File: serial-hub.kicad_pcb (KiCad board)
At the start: 2 copper layers, 100 x 100 mm, 63 parts, among them J1 USB_C_Receptacle_USB2.0, J10 RJ45_LED_Shielded, J2 Conn_01x04_Male, J3 Conn_01x03_Male, J4 Conn_01x03_Male, J5 RJ45_LED_Shielded, J6 RJ45_LED_Shielded, J7 Conn_01x03_Male, J8 Conn_01x03_Male, J9 RJ45_LED_Shielded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

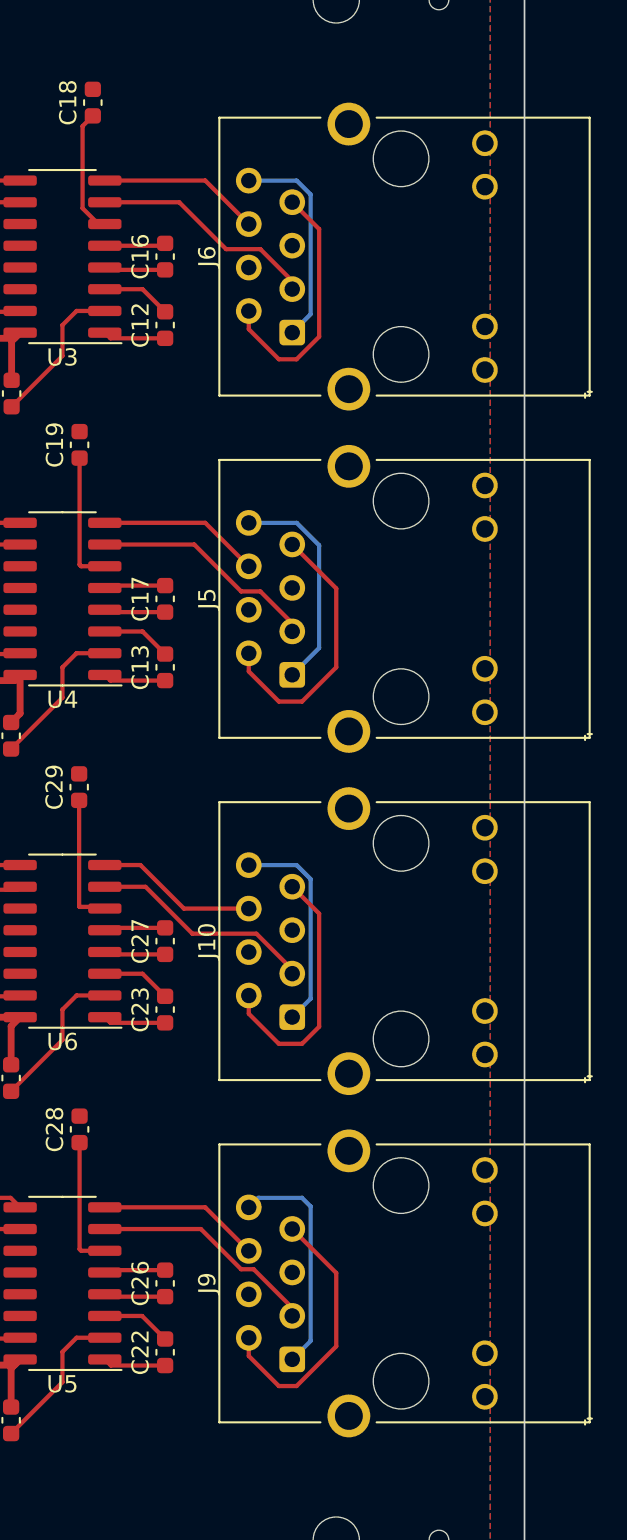
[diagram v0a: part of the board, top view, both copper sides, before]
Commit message: board: fix wrong RJ45 pins
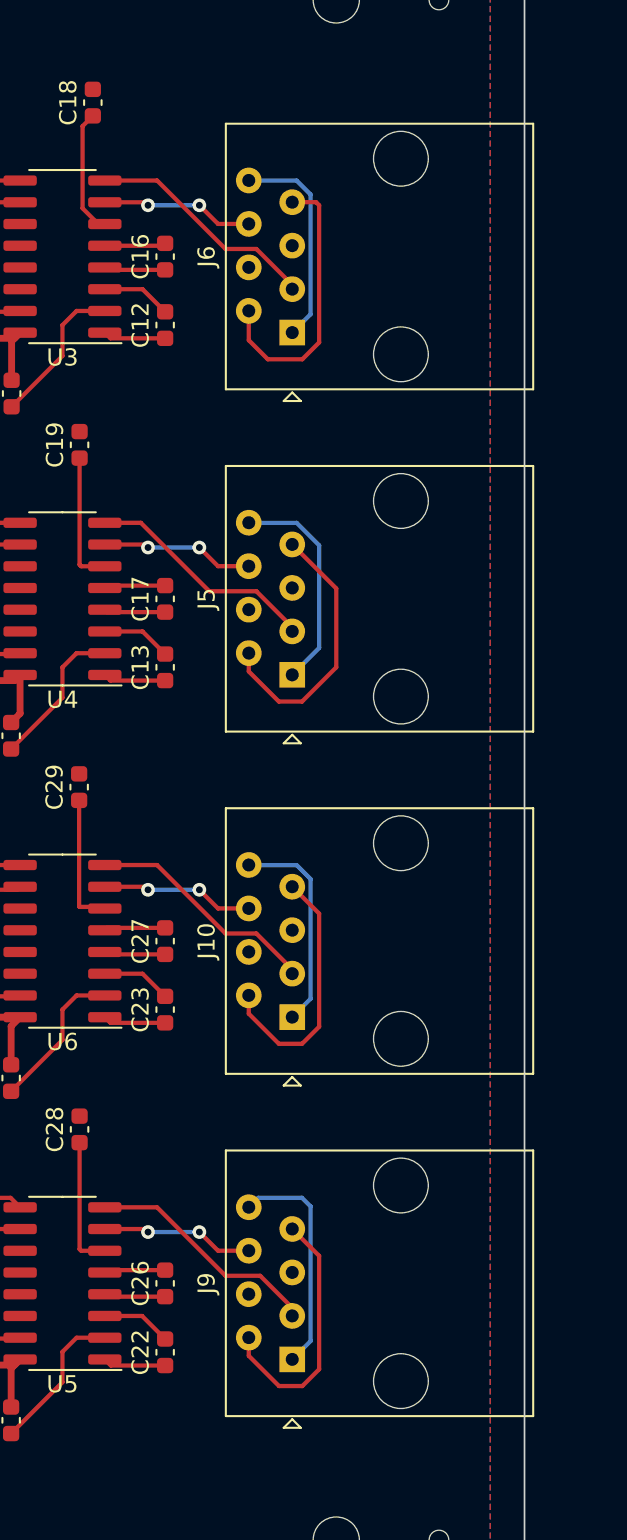
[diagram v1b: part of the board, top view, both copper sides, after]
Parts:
- J10, J5, J6, J9: footprint Connector_RJ:RJ45_Hanrun_HR911105A -> Connector_RJ:RJ45_Amphenol_54602-x08_Horizontal
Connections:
- J10 pad 3: /P2_TX -> /P2_RX
- J10 pad 6: /P2_RX -> /P2_TX
- J5 pad 3: /P1_TX -> /P1_RX
- J5 pad 6: /P1_RX -> /P1_TX
- J6 pad 3: /P0_TX -> /P0_RX
- J6 pad 6: /P0_RX -> /P0_TX
- J9 pad 3: /P3_TX -> /P3_RX
- J9 pad 6: /P3_RX -> /P3_TX
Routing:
- net /P1_RX: track 9.47 -> 14.2 mm
- net /P0_RX: track 9.47 -> 14.2 mm
- net /P3_TX: track 13.3 -> 8.94 mm, vias 0 -> 2
- net /P0_TX: track 13.3 -> 8.94 mm, vias 0 -> 2
- net /P1_TX: track 13.3 -> 8.94 mm, vias 0 -> 2
- net /P3_RX: track 9.47 -> 13.9 mm
- net /P2_RX: track 9.47 -> 13.7 mm
- net /P2_TX: track 13.2 -> 8.94 mm, vias 0 -> 2
- net Net-(J6-Pad2): track 15.0 -> 16.4 mm
- net Net-(J9-Pad2): track 15.8 -> 15.2 mm
